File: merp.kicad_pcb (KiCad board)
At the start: 2 copper layers, 100 x 45.7 mm, 27 parts, among them J1 A, J10 -12V, J11 F, J12 Conn_01x04_Male, J2 B, J3 C, J4 D, J5 E, J6 IO1, J7 IO2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

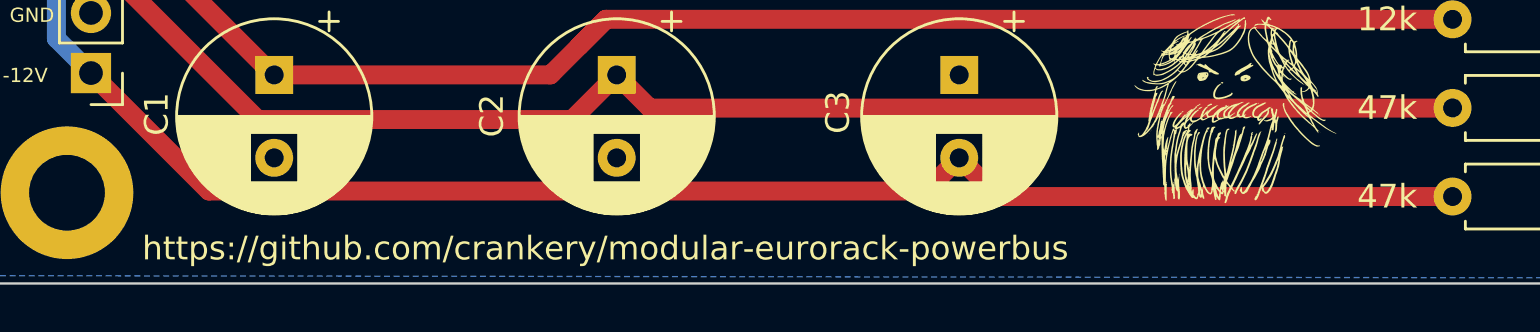
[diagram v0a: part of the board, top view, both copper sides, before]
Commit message: fix url on board
upgrade to kicad 7
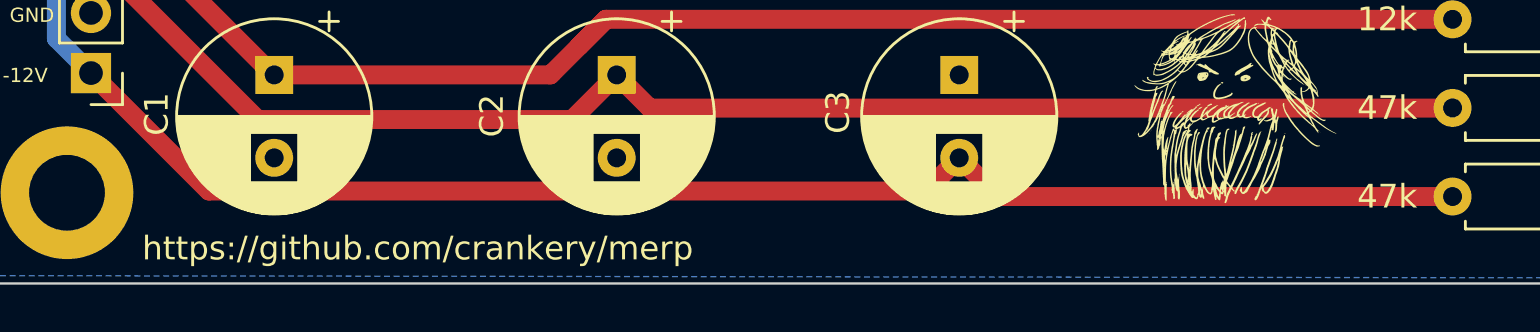
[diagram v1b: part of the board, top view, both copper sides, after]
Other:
- board text added: "https://github.com/crankery/merp"
- board text removed: "https://github.com/crankery/modular-eurorack-powerbus"
